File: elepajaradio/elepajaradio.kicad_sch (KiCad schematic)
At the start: 29 parts, among them J1 SPI, J2 UART, J3 vdd_gnd, J4 reset, SW1 RotaryEncoder, SW2 SW_Push, SW3 SW_Push, U1 MAX2606, U2 OLED_I2C, U3 ATmega328PB-A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

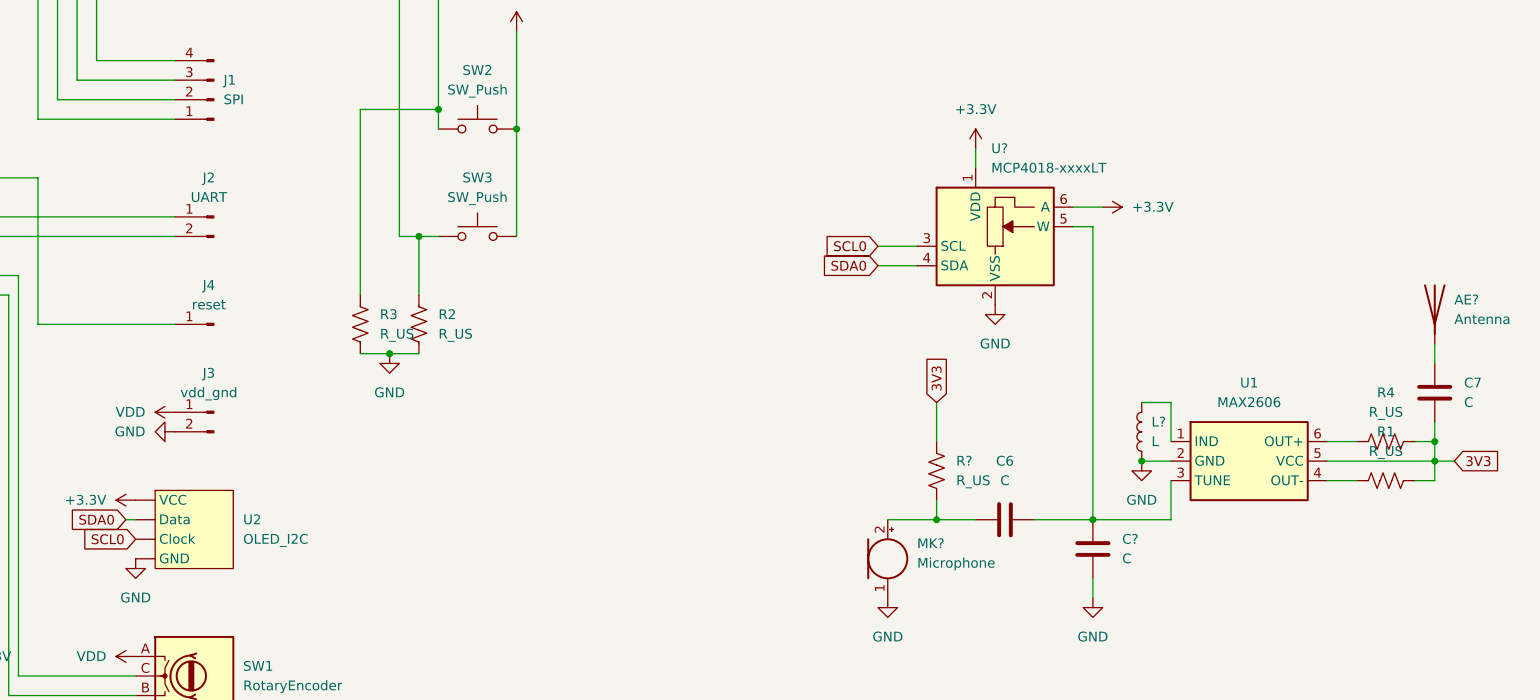
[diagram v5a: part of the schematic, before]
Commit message: initial pcb design and adding antenna connector
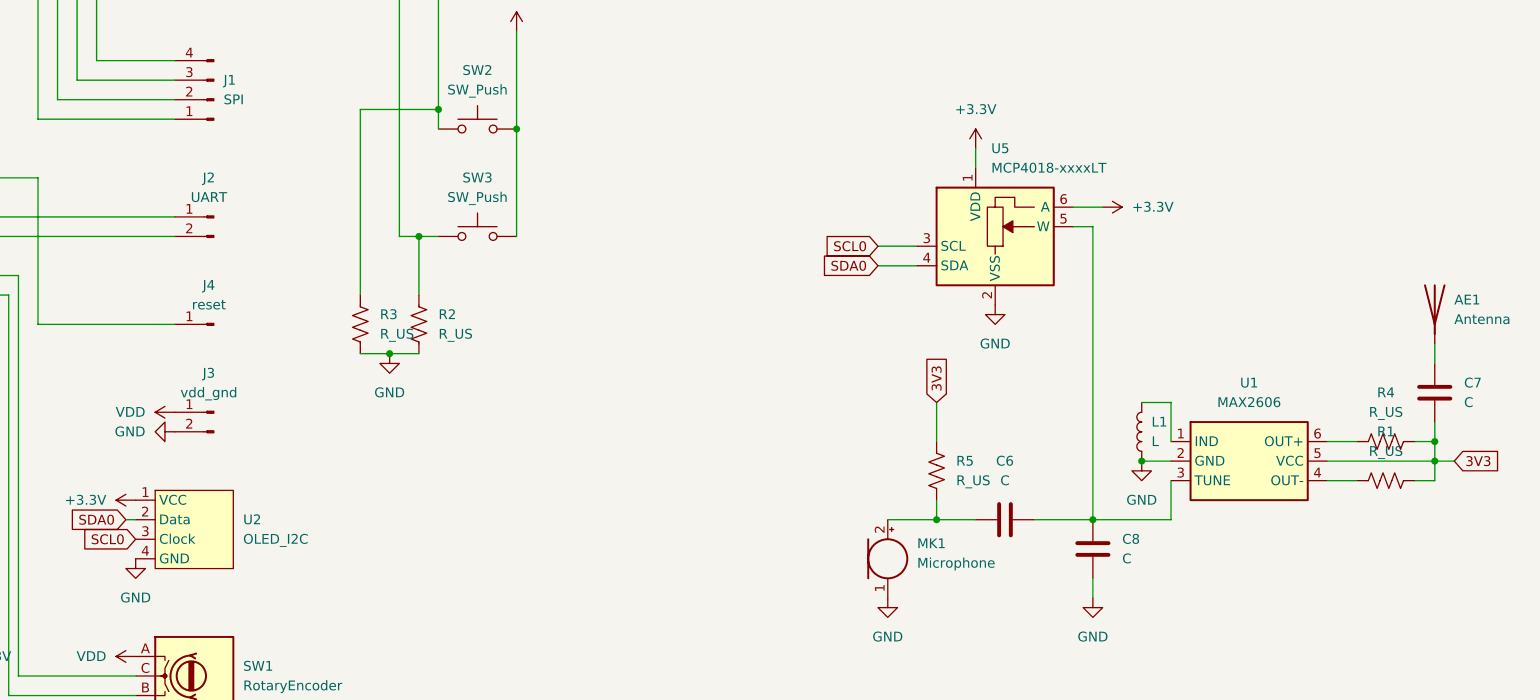
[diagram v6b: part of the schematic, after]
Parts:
- AE1: renamed from AE?; footprint (none) -> Connector_Coaxial:BNC_TEConnectivity_1478204_Vertical
- SW2, SW3: footprint (none) -> Connector_PinHeader_2.54mm:PinHeader_1x02_P2.54mm_Vertical
- U1: footprint (none) -> Package_TO_SOT_SMD:SOT-23-6
- Y1: footprint Oscillator:Oscillator_SMD_Abracon_ASDMB-4Pin_2.5x2.0mm -> Crystal:Crystal_HC18-U_Vertical
- gave numbers to parts that had none: 5
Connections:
- net +3.3V: now also U2.1 (VCC); no longer U2. (VCC)
- net GND: now also U2.4 (GND); no longer U2. (VCC)
- net SCL0: now also U2.3 (Clock); no longer U2. (VCC)
- net SDA0: now also U2.2 (Data); no longer U2. (VCC)
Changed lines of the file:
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@@
       (effects (font (size 1.27 1.27)) (justify left))
     )
-    (property "Footprint" "Connector_PinHeader_2.54mm:PinHeader_1x04_P2.54mm_Vertical" (at 91.44 116.84 0)
+    (property "Footprint" "Connector_PinHeader_2.54mm:PinHeader_1x04_P2.54mm_Vertical" (at 92.71 109.22 0)
       (effects (font (size 1.27 1.27)) hide)
     )
@@
       (effects (font (size 1.27 1.27)) hide)
     )
-    (pin "")
-    (pin "")
-    (pin "")
-    (pin "")
+    (pin "1")
+    (pin "2")
+    (pin "3")
+    (pin "4")
     (instances
       (project "elepajaradio"
@@
       (effects (font (size 1.27 1.27)) (justify right))
     )
-    (property "Footprint" "Oscillator:Oscillator_SMD_Abracon_ASDMB-4Pin_2.5x2.0mm" (at 97.79 31.75 0)
+    (property "Footprint" "Crystal:Crystal_HC18-U_Vertical" (at 97.79 31.75 0)
       (effects (font (size 1.27 1.27)) hide)
     )
@@
   (symbol (lib_id "power:GND") (at 180.34 124.46 0) (unit 1)
     (in_bom yes) (on_board yes) (dnp no) (fields_autoplaced)
-    (property "Reference" "#PWR?" (at 180.34 130.81 0)
+    (property "Reference" "#PWR0105" (at 180.34 130.81 0)
       (effects (font (size 1.27 1.27)) hide)
     )
@@
       (project "elepajaradio"
         (path "/be645d0f-8568-47a0-a152-e3ddd33563eb"
-          (reference "#PWR?") (unit 1)
+          (reference "#PWR0105") (unit 1)
         )
       )
@@
   (symbol (lib_id "power:GND") (at 213.36 106.68 0) (unit 1)
     (in_bom yes) (on_board yes) (dnp no) (fields_autoplaced)
-    (property "Reference" "#PWR?" (at 213.36 113.03 0)
+    (property "Reference" "#PWR0102" (at 213.36 113.03 0)
       (effects (font (size 1.27 1.27)) hide)
     )
@@
       (project "elepajaradio"
         (path "/be645d0f-8568-47a0-a152-e3ddd33563eb"
-          (reference "#PWR?") (unit 1)
+          (reference "#PWR0102") (unit 1)
         )
       )
@@
   (symbol (lib_id "Device:Antenna") (at 251.46 86.36 0) (unit 1)
     (in_bom yes) (on_board yes) (dnp no) (fields_autoplaced)
-    (property "Reference" "AE?" (at 254 85.7249 0)
+    (property "Reference" "AE1" (at 254 85.7249 0)
       (effects (font (size 1.27 1.27)) (justify left))
     )
@@
       (effects (font (size 1.27 1.27)) (justify left))
     )
-    (property "Footprint" "" (at 251.46 86.36 0)
+    (property "Footprint" "Connector_Coaxial:BNC_TEConnectivity_1478204_Vertical" (at 251.46 86.36 0)
       (effects (font (size 1.27 1.27)) hide)
     )
@@
       (project "elepajaradio"
         (path "/be645d0f-8568-47a0-a152-e3ddd33563eb"
-          (reference "AE?") (unit 1)
+          (reference "AE1") (unit 1)
         )
       )
@@
   (symbol (lib_id "Device:R_US") (at 186.69 107.95 180) (unit 1)
     (in_bom yes) (on_board yes) (dnp no) (fields_autoplaced)
-    (property "Reference" "R?" (at 189.23 106.6799 0)
+    (property "Reference" "R5" (at 189.23 106.6799 0)
       (effects (font (size 1.27 1.27)) (justify right))
     )
@@
       (project "elepajaradio"
         (path "/be645d0f-8568-47a0-a152-e3ddd33563eb"
-          (reference "R?") (unit 1)
+          (reference "R5") (unit 1)
         )
       )
@@
       (effects (font (size 1.27 1.27)))
     )
-    (property "Footprint" "" (at 227.33 105.41 0)
+    (property "Footprint" "Package_TO_SOT_SMD:SOT-23-6" (at 227.33 105.41 0)
       (effects (font (size 1.27 1.27)) hide)
     )
@@
   (symbol (lib_id "Device:Microphone") (at 180.34 119.38 0) (unit 1)
     (in_bom yes) (on_board yes) (dnp no) (fields_autoplaced)
-    (property "Reference" "MK?" (at 184.15 117.4114 0)
+    (property "Reference" "MK1" (at 184.15 117.4114 0)
       (effects (font (size 1.27 1.27)) (justify left))
     )
@@
       (project "elepajaradio"
         (path "/be645d0f-8568-47a0-a152-e3ddd33563eb"
-          (reference "MK?") (unit 1)
+          (reference "MK1") (unit 1)
         )
       )
@@
       (effects (font (size 1.27 1.27)))
     )
-    (property "Footprint" "" (at 127 72.39 0)
+    (property "Footprint" "Connector_PinHeader_2.54mm:PinHeader_1x02_P2.54mm_Vertical" (at 127 72.39 0)
       (effects (font (size 1.27 1.27)) hide)
     )
@@
       (effects (font (size 1.27 1.27)))
     )
-    (property "Footprint" "" (at 127 58.42 0)
+    (property "Footprint" "Connector_PinHeader_2.54mm:PinHeader_1x02_P2.54mm_Vertical" (at 127 58.42 0)
       (effects (font (size 1.27 1.27)) hide)
     )
@@
   (symbol (lib_id "power:GND") (at 194.31 86.36 0) (unit 1)
     (in_bom yes) (on_board yes) (dnp no) (fields_autoplaced)
-    (property "Reference" "#PWR?" (at 194.31 92.71 0)
+    (property "Reference" "#PWR0101" (at 194.31 92.71 0)
       (effects (font (size 1.27 1.27)) hide)
     )
@@
       (project "elepajaradio"
         (path "/be645d0f-8568-47a0-a152-e3ddd33563eb"
-          (reference "#PWR?") (unit 1)
+          (reference "#PWR0101") (unit 1)
         )
       )
@@
   (symbol (lib_id "Device:C") (at 207.01 118.11 0) (unit 1)
     (in_bom yes) (on_board yes) (dnp no) (fields_autoplaced)
-    (property "Reference" "C?" (at 210.82 116.8399 0)
+    (property "Reference" "C8" (at 210.82 116.8399 0)
       (effects (font (size 1.27 1.27)) (justify left))
     )
@@
       (project "elepajaradio"
         (path "/be645d0f-8568-47a0-a152-e3ddd33563eb"
-          (reference "C?") (unit 1)
+          (reference "C8") (unit 1)
         )
       )
@@
   (symbol (lib_id "Device:L") (at 213.36 102.87 180) (unit 1)
     (in_bom yes) (on_board yes) (dnp no) (fields_autoplaced)
-    (property "Reference" "L?" (at 214.63 101.5999 0)
+    (property "Reference" "L1" (at 214.63 101.5999 0)
       (effects (font (size 1.27 1.27)) (justify right))
     )
@@
       (project "elepajaradio"
         (path "/be645d0f-8568-47a0-a152-e3ddd33563eb"
-          (reference "L?") (unit 1)
+          (reference "L1") (unit 1)
         )
       )
@@
   (symbol (lib_id "power:GND") (at 207.01 124.46 0) (unit 1)
     (in_bom yes) (on_board yes) (dnp no) (fields_autoplaced)
-    (property "Reference" "#PWR?" (at 207.01 130.81 0)
+    (property "Reference" "#PWR0104" (at 207.01 130.81 0)
       (effects (font (size 1.27 1.27)) hide)
     )
@@
       (project "elepajaradio"
         (path "/be645d0f-8568-47a0-a152-e3ddd33563eb"
-          (reference "#PWR?") (unit 1)
+          (reference "#PWR0104") (unit 1)
         )
       )
@@
   (symbol (lib_id "Potentiometer_Digital:MCP4018-xxxxLT") (at 194.31 78.74 0) (unit 1)
     (in_bom yes) (on_board yes) (dnp no) (fields_autoplaced)
-    (property "Reference" "U?" (at 193.7894 66.04 0)
+    (property "Reference" "U5" (at 193.7894 66.04 0)
       (effects (font (size 1.27 1.27)) (justify left))
     )
@@
       (project "elepajaradio"
         (path "/be645d0f-8568-47a0-a152-e3ddd33563eb"
-          (reference "U?") (unit 1)
-        )
-      )
+          (reference "U5") (unit 1)
+        )
+      )
